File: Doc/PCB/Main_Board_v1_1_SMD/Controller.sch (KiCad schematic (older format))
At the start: 69 parts, among them J11 UART, J12 I2C Interface LCD_C, J13 BUZZER_C, J24 Conn_01x08, J25 POWEROFF, J7 TE_3.5mm_Screwless_P2, J8 SV2, J9 SV3, Q2 FDT1600N10ALZ, Q3 FDT1600N10ALZ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

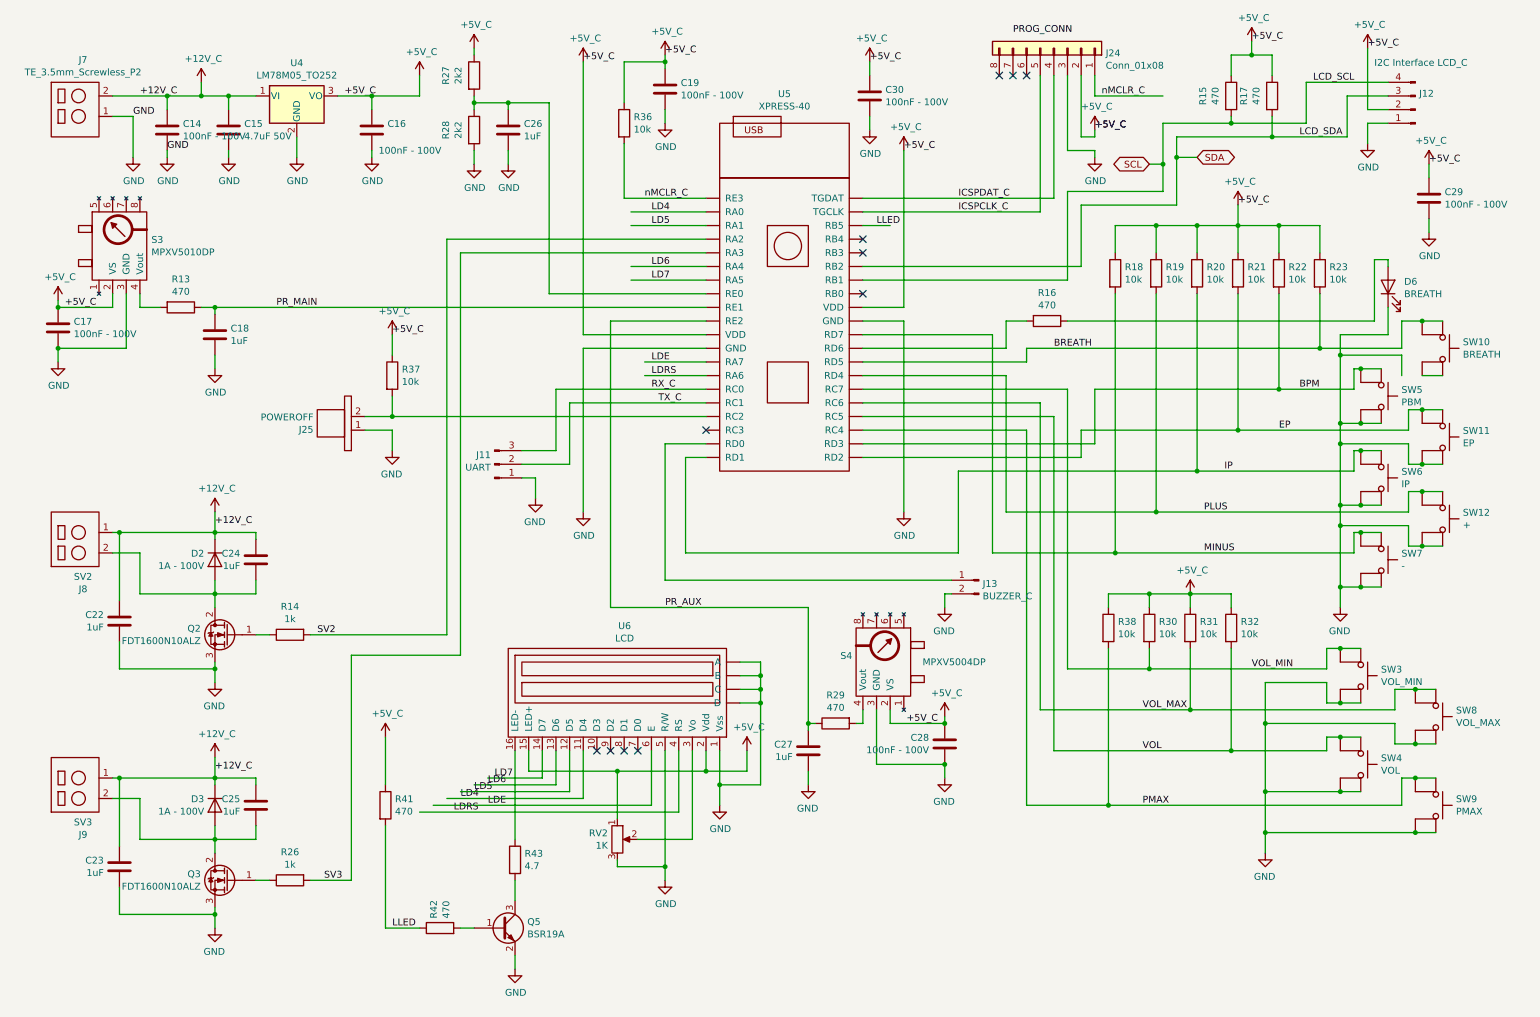
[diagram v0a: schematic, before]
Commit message: First tests with artificial lung. 70 cases. New PCB THT fixing mounting issues
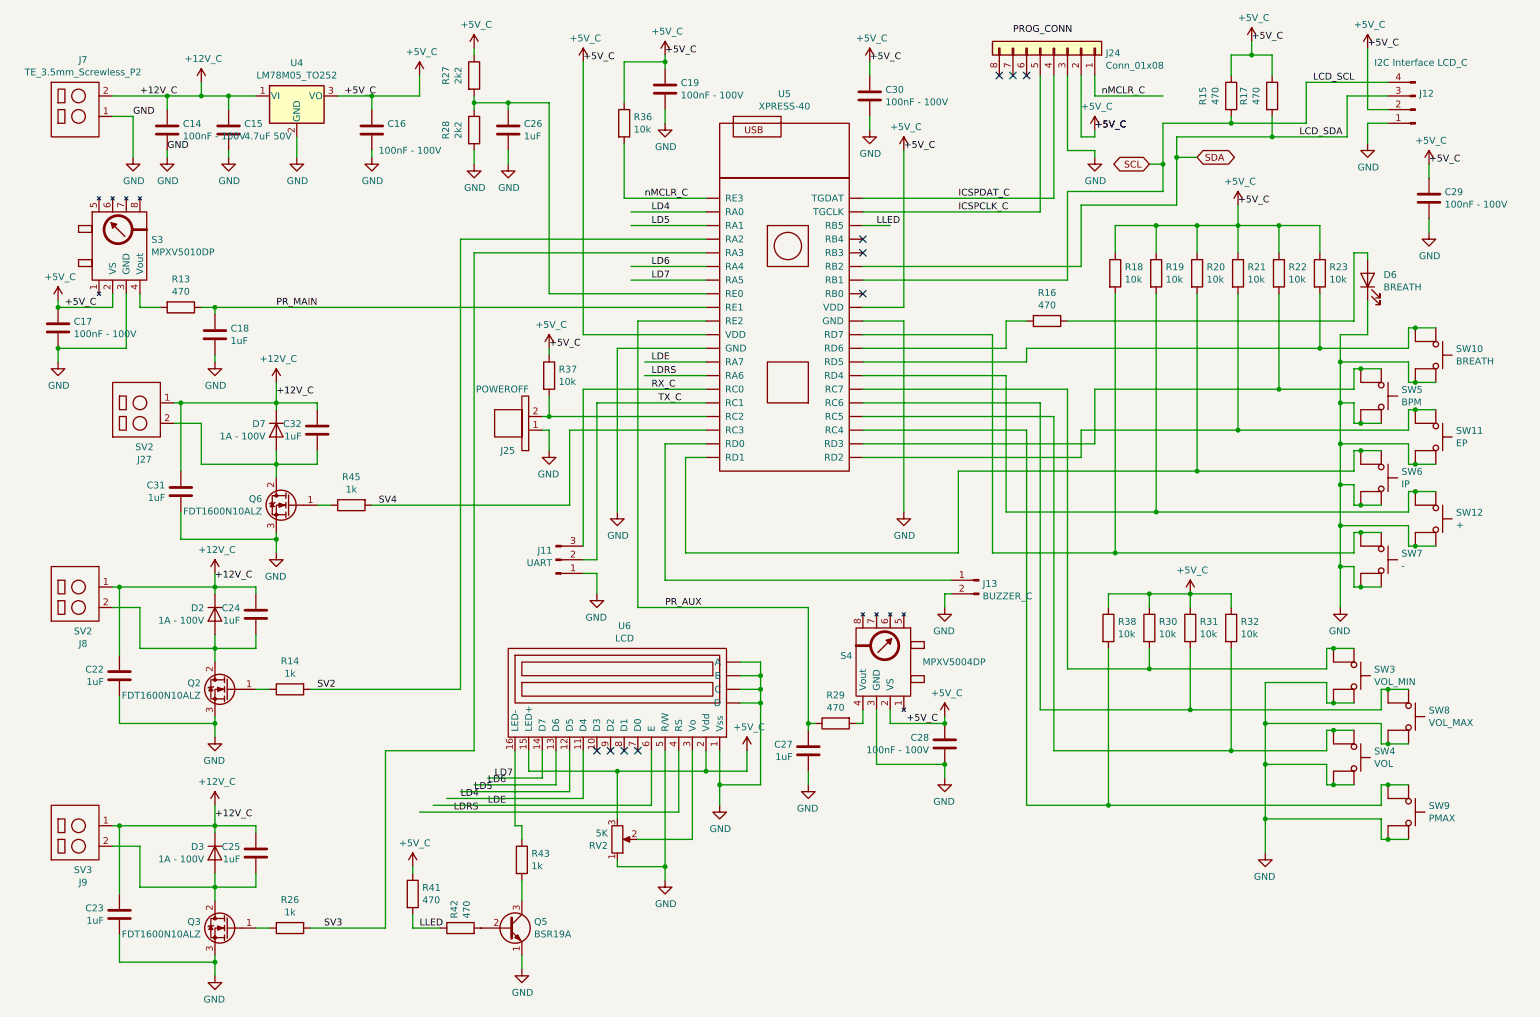
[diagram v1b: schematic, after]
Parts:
- removed Q5: BSR19A, Package_TO_SOT_SMD:TSOT-23, symbol Ventilator:BSR19A
- removed U4: LM78M05_TO252, Package_TO_SOT_SMD:TO-252-2, symbol Regulator_Linear:LM78M05_TO252
- added C31, C32: 1uF, Capacitor_SMD:C_1206_3216Metric_Pad1.42x1.75mm_HandSolder, symbol Device:C
- added D7: 1A - 100V, Diode_SMD:D_SMA-SMB_Universal_Handsoldering, symbol Diode:1N4001
- added J27: SV2, Ventilator:PinHeader_1x02_Screwless_3.5mm, symbol Ventilator:TE_3.5mm_Screwless_P2
- added Q5: BSR19A, Package_TO_SOT_SMD:TSOT-23, symbol Transistor_BJT:2N3904
- added Q6: FDT1600N10ALZ, Package_TO_SOT_SMD:SOT-223-3_TabPin2, symbol Transistor_FET:IRLZ34N
- added R45: 1k, Resistor_SMD:R_0603_1608Metric_Pad1.05x0.95mm_HandSolder, symbol Device:R
- added U4: LM78M05_TO252, Package_TO_SOT_SMD:TO-252-2, symbol Regulator_Linear:LM7805_TO220
- R43: value 4.7 -> 1k
- RV2: value 1K -> 5K; footprint Ventilator:Potentiometer_409HA -> Potentiometer_SMD:Potentiometer_Vishay_TS53YJ_Vertical
- SW5: value PBM -> BPM
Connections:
- net labels added: SV4
- net labels removed: BPM, BREATH, EP, IP, MINUS, PLUS, PMAX, VOL, VOL_MAX, VOL_MIN
- wire segments 381 -> 414
- no-connect marks 11 -> 10
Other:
- moved on the sheet: C22, C23, C24, C25, D2, D3, J11, J25, J8, J9, Q2, Q3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

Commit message: New SMD PCB
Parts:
- U5: footprint Package_DFN_QFN:UQFN-40-1EP_5x5mm_P0.4mm_EP3.8x3.8mm_ThermalVias -> Package_DFN_QFN:UQFN-40-1EP_5x5mm_P0.4mm_EP3.8x3.8mm
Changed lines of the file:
@@
 F 0 "U5" H 6075 3315 50  0000 C CNN
 F 1 "XPRESS-40" H 6075 3224 50  0000 C CNN
-F 2 "Package_DFN_QFN:UQFN-40-1EP_5x5mm_P0.4mm_EP3.8x3.8mm_ThermalVias" H 6400 2200 50  0001 C CNN
+F 2 "Package_DFN_QFN:UQFN-40-1EP_5x5mm_P0.4mm_EP3.8x3.8mm" H 6400 2200 50  0001 C CNN
 F 3 "https://es.rs-online.com/web/p/microcontroladores/1717862/" H 6400 2200 50  0001 C CNN
 	1    6400 2200
